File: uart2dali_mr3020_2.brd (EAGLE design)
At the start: 52 x 70 mm, 62 parts, among them IC1 SFH6156, IC2 SFH6156, IC4 7805DT, J1 AVR_SPI_PRG_6NS, Q1 BC817-25SMD, X2 SM04B-SRSS-TB

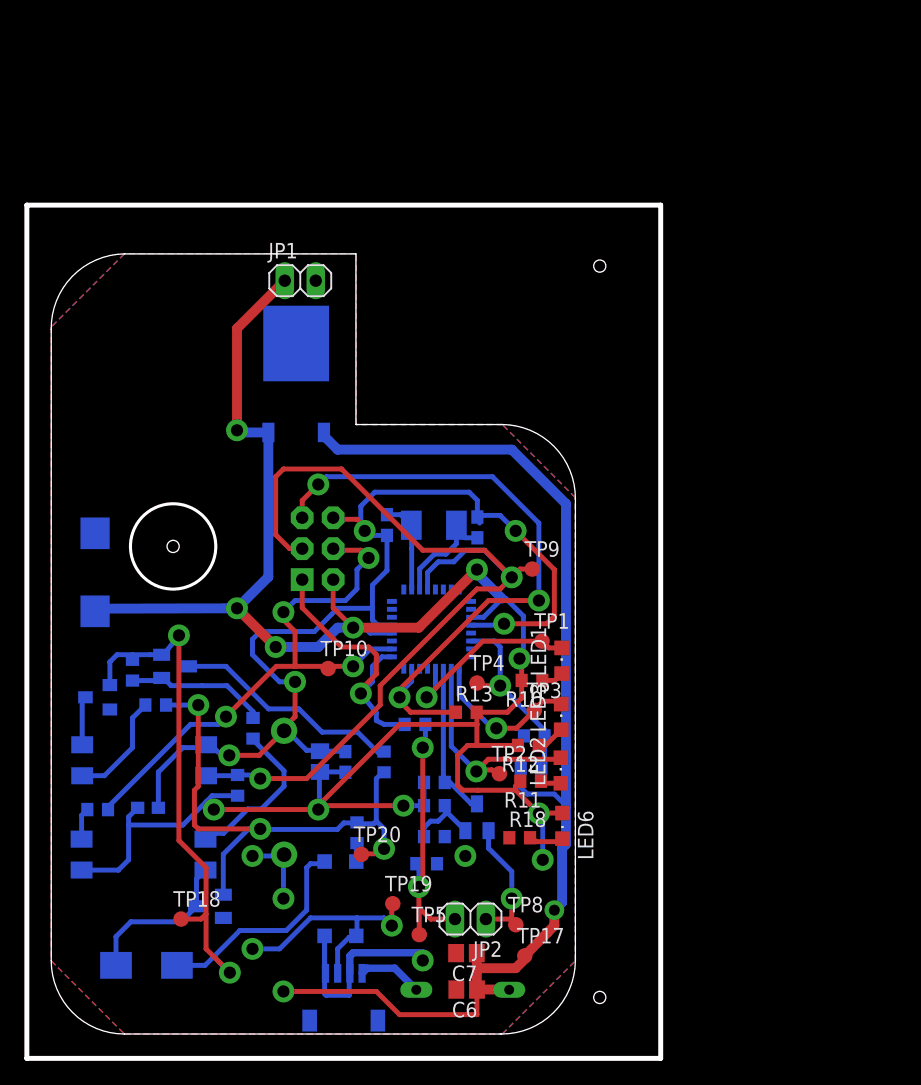
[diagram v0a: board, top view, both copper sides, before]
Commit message: working on uart2dali board version 2 with switching voltage regulators
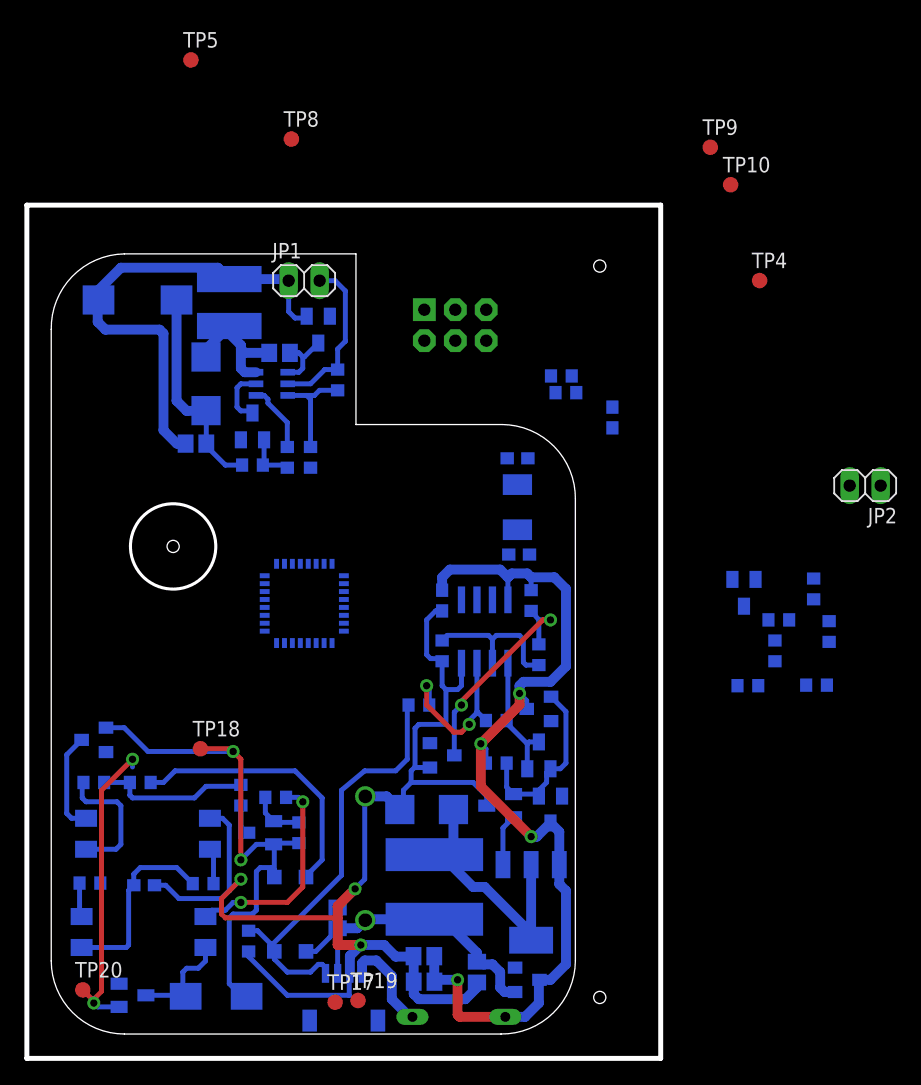
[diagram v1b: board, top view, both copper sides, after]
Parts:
- removed LED1, LED2, LED3, LED6: (no value), led:CHIPLED_0805
- removed TP1, TP2, TP3: TPB1,27, testpad:B1,27
- added C10: (no value), resistor:C0603
- added C11, C13: (no value), resistor:C0805
- added C12: (no value), resistor:CT6032
- added D10: BAS40, diode:SOT23
- added D11, D5, D6, D8: BZX84CSMD, diode:TO236
- added D7: MBRS130LT3, diode:SMB
- added D9: BZX85, diode:DO41Z10
- added IC3: SFH6156, optocoupler:SFH
- added Q2: BSP170P, transistor-fet:SOT223
- added Q3: BC817-25SMD, transistor-npn:SOT23-BEC
- added R22, R23, R24, R25, R26: (no value), resistor:R0603
- added T2, T3: (no value), transistor:SOT23-BEC
- added U$2: AT90PWM316, at90pwm316:QFN32_7MM
- added U$3: SDR0805, inductor:SDR0805
- C1: device resistor:CT6032 -> resistor:C0805
- C2, C3: device resistor:C0603 -> resistor:C0805
- C4: device resistor:CT7343 -> resistor:C0805
- C5: device resistor:C0603 -> resistor:CT7343
- C6, C7, C8: device resistor:C0805 -> resistor:C0603
- D1: value BAS40 -> 1N4148DO35-7; device diode:SOT23 -> diode:DO35-7
- D2: value BZX84CSMD -> BAS40; device diode:TO236 -> diode:SOT23
- D3: value BZX85 -> MBRS130LT3; device diode:DO41Z10 -> diode:SMB
- D4: value 1N4148DO35-7 -> BAS40; device diode:DO35-7 -> diode:SOT23
- IC1: value SFH6156 -> (none); device optocoupler:SFH -> ltc_swr:SOT23-6
- IC2: value SFH6156 -> LM393D; device optocoupler:SFH -> linear:SO08
- IC4: value 7805DT -> SFH6156; device linear:TO252 -> optocoupler:SFH
- Q1: value BC817-25SMD -> SST201; device transistor-npn:SOT23-BEC -> transistor-fet:SOT23
- R1, R2: device resistor:0204/7 -> resistor:R0603
- U$1: value AT90PWM316 -> KMP_2330_UNSHIELDED; device at90pwm316:QFN32_7MM -> inductor:KMP_2330_UNSHIELDED
- moved TP5 74.2 mm to (11.5, 79.9)
- moved TP8 67.0 mm to (19.7, 73.4)
- moved R8 57.1 mm to (59.4, 31.4), turned to 90 degrees
- moved R7 56.1 mm to (62.8, 28.6), turned to 0 degrees
- moved D4 55.4 mm to (21.9, 57.8), turned to 180 degrees
- moved TP10 51.6 mm to (55.7, 69.7)
- moved JP2 48.1 mm to (66.8, 45.0)
- moved R6 47.4 mm to (62.5, 36.5)
- moved R9 42.7 mm to (57.1, 28.6), turned to 0 degrees
- moved R5 42.1 mm to (63.8, 33.0)
- moved C5 41.7 mm to (7.08, 60.2)
- moved C7 40.8 mm to (38.3, 47.2), flipped to the bottom, turned to 0 degrees
- moved TP4 40.3 mm to (58.1, 61.8)
- moved IC1 40.0 mm to (18.1, 53.3)
- moved IC4 39.6 mm to (7.94, 16.4), turned to 270 degrees
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- renumbered X2 to X1
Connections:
- removed net N$13: B1.-, R5.1
- removed net N$14: LED2.A, R11.1
- removed net N$15: LED3.A, R12.1
- removed net N$21: R20.1, T1.C, U$1.P27
- removed net N$27: LED3.C, TP3.TP, U$1.P25
- removed net N$28: LED2.C, TP2.TP, U$1.P26
- removed net N$29: LED1.C, TP1.TP, U$1.P28
- removed net N$30: R16.1, R17.2, TP4.TP, U$1.P22
- removed net N$32: LED6.C, R18.2
- removed net N$7: B1.+, C1.-, D2.A, Q1.E, R7.2, TP18.TP
- removed net N$8: LED1.A, R10.1
- new net D+: B1.+, C12.-, D11.A, Q3.E, R22.2, TP18.TP
- new net D-: B1.-, R23.1
- new net GNDA: B1.~2, R17.1, R19.2, X1.4
- new net N$18: IC1.4, R2.1
- new net N$22: IC2.1, Q1.2, Q1.3, R16.1
- new net N$24: C3.1, D4.3, IC1.1
- new net N$25: C3.2, D3.C, IC1.6, U$1.P$2
- new net N$26: D7.C, Q2.2, Q2.4, U$3.P$2
- new net N$31: IC1.3, R3.2, R4.2
- new net N$33: Q2.1, T2.E, T3.E
- new net N$34: D6.A, Q1.1, R18.1, T2.B, T3.B
- new net N$35: D5.C, R13.1, R14.1
- new net N$40: IC2.3, R16.2, R17.2
- new net SOFT_RXD_5V: R10.1, T1.C, U$2.P27
- new net VCC/2: B1.~1, C11.1, C13.2, D8.A, D9.C, TP19.TP, U$3.P$1, X1.3
- new net V_SENSE: R11.1, R12.2, TP4.TP, U$2.P22
- net +5V: now also C4.2, C5.+, C6.2, D4.1, IC3.1, R26.1, R4.1, R7.2, R9.2, U$1.P$1, U$2.P19, U$2.P4; no longer C4.+, C5.2, C8.2, IC1.1, IC4.2, LED6.A, R11.2, R12.2, R13.2, R19.2, R20.2, R9.1, U$1.P19, U$1.P4
- net DALI_RCV: now also IC4.4, R26.2, U$2.P12; no longer IC2.4, R9.2, U$1.P12
- net DALI_TRM: now also R20.1, U$2.P2; no longer R8.1, U$1.P2
- net GND: now also C1.2, C10.2, C11.2, C13.1, C2.2, C4.1, C5.-, C6.1, C7.1, D5.A, D7.A, D9.A, IC1.2, IC2.4, R1.2, R12.1, R15.2, R19.1, R3.1, R5.1, R8.2, T3.C, U$2.P20, U$2.P5; no longer B1.~2, C2.1, C3.1, C4.-, C5.1, C6.2, C7.2, IC2.3, R15.1, R17.1, R18.1, R21.2, U$1.P20, U$1.P5, X1.4
- net MISO: now also R6.2, U$2.P1; no longer R14.2, U$1.P1
- net N$1: now also IC3.2, R20.2; no longer IC1.2, R8.2
- net N$10: now also Q3.C, R24.2; no longer Q1.C, R3.2
- net N$11: now also IC4.1, R25.1; no longer IC2.1, R4.1
- net N$12: now also D11.C, IC4.2; no longer D2.C, IC2.2
- net N$16: now also C7.2, U$2.P10; no longer C2.2, U$1.P10
- net N$19: now also C8.2, U$2.P11; no longer C3.2, U$1.P11
- net N$2: now also IC2.2, R14.2, R15.1; no longer B1.~1, R2.1, TP19.TP, X1.3
- net N$20: now also R8.1, R9.1; no longer R19.1, R21.1
- net N$23: now also D1.A; no longer D4.A
- net N$3: now also D2.3, IC1.5; no longer D3.C, R1.1, R2.2
- net N$4: now also C12.+, D10.3, IC3.4; no longer C1.+, D1.3, IC1.4
- net N$5: now also IC3.3, R21.1; no longer IC1.3, R6.1
- net N$6: now also Q3.B, R21.2, R22.1; no longer Q1.B, R6.2, R7.1
- net N$9: now also D10.1, R23.2, R24.1, R25.2; no longer D1.1, R3.1, R4.2, R5.2
- net RESET: now also R7.1, U$2.P31; no longer R13.1, U$1.P31
- net SOFT_TXD: now also R5.2, R6.1; no longer R14.1, R15.2
- net VDD: now also C1.1, C10.1, C2.1, D1.C, D2.1, D6.C, D8.C, IC2.8, Q2.3, R1.1, R11.2, R13.2, R18.2, R2.2, T2.C; no longer C6.1, C7.1, D4.C, IC4.1, R1.2, R16.2
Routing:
- net +5V: track 181.3 -> 55.3 mm, vias 11 -> 0
- net DALI_RCV: track 75.7 -> 2.94 mm, vias 2 -> 0
- net N$7: track 60.2 -> 0.00 mm, vias 2 -> 0
- net RESET: track 52.7 -> 0.00 mm, vias 3 -> 0
- net DALI_TRM: track 47.3 -> 0.00 mm, vias 4 -> 0
- net D+: track 0.00 -> 46.4 mm, vias 0 -> 2
- net GNDA: track 0.00 -> 35.4 mm
- net GND: track 110.9 -> 143.1 mm, vias 7 -> 3
- net VCC/2: track 0.00 -> 25.6 mm
- net MISO: track 23.3 -> 0.00 mm, vias 1 -> 0
- net SOFT_TXD: track 22.7 -> 0.00 mm, vias 2 -> 0
- net D-: track 0.00 -> 22.4 mm
- net N$26: track 0.00 -> 21.8 mm
- net N$35: track 0.00 -> 18.7 mm, vias 0 -> 2
- net N$28: track 18.5 -> 0.00 mm, vias 1 -> 0
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- removed copper zone on layer 1, net GND
- removed copper zone on layer 16, net GND

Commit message: new version of the base board with 2 switching regulators
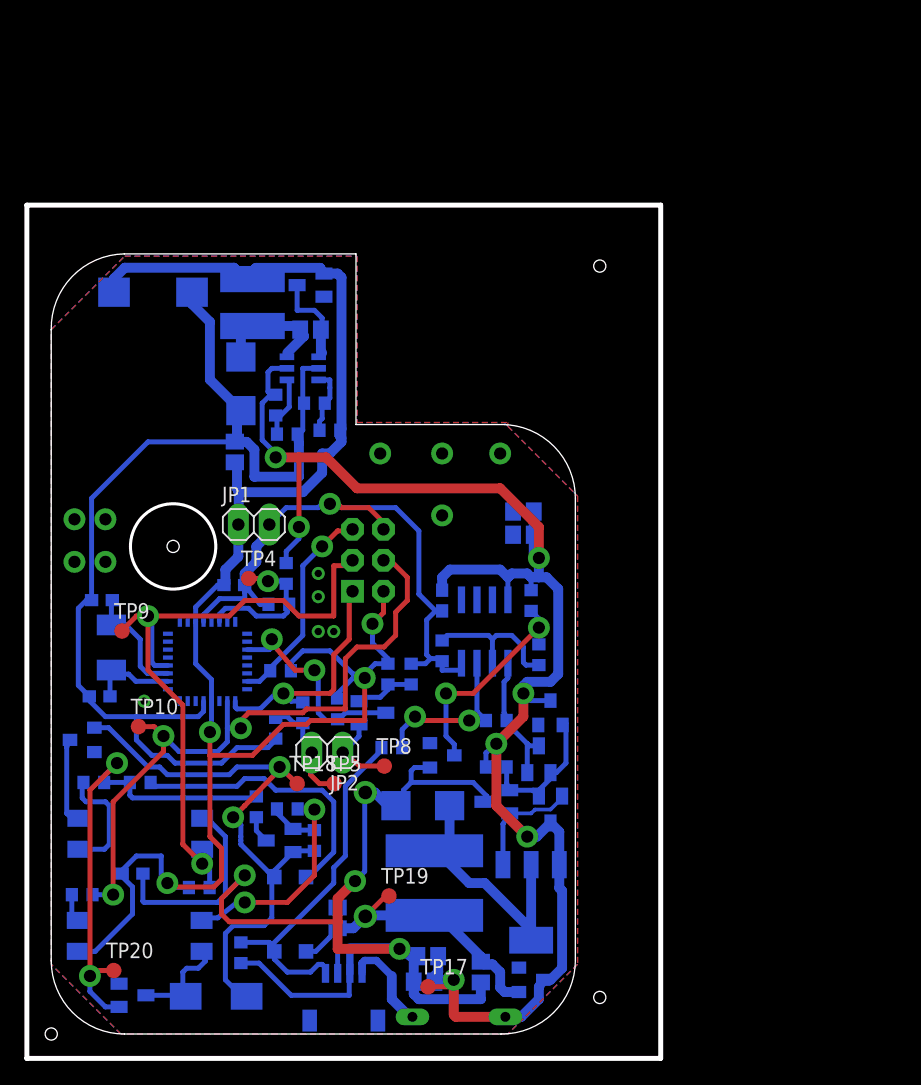
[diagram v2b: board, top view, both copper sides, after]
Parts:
- removed D2: BAS40, diode:SOT23
- added C14, C15: (no value), resistor:C0805
- R1: value (none) -> 10k
- R2: value (none) -> 47k
- R3: value (none) -> 27k
- R4: value (none) -> 82k
- moved TP10 65.8 mm to (7.16, 25.2)
- moved TP9 62.5 mm to (5.81, 33.1)
- moved TP5 60.5 mm to (23.2, 20.5)
- moved TP8 52.0 mm to (27.3, 22.0)
- moved JP2 49.3 mm to (22.6, 23.1)
- moved TP4 48.5 mm to (16.2, 37.4)
- moved R5 46.1 mm to (18.4, 25.1)
- moved R7 44.0 mm to (18.8, 29.8), turned to 180 degrees
- moved R6 43.1 mm to (20.6, 26.4)
- moved C7 39.5 mm to (3.97, 27.7), turned to 180 degrees
- moved R10 36.9 mm to (23.5, 26.7), turned to 90 degrees
- moved Y1 35.2 mm to (4.93, 31.7), turned to 270 degrees
- moved C8 34.4 mm to (4.16, 35.6), turned to 180 degrees
- moved C9 33.9 mm to (15.0, 36.8), turned to 180 degrees
- moved T1 32.0 mm to (26.4, 26.4), turned to 90 degrees
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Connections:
- removed net N$18: IC1.4, R2.1
- net GND: now also C14.2, C15.2
- net N$3: now also IC1.4, R1.1, R2.1; no longer D2.3, IC1.5
- net VDD: now also C14.1, C15.1, IC1.5; no longer D2.1, R1.1
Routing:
- net GND: track 143.1 -> 244.0 mm, vias 3 -> 17
- net +5V: track 55.3 -> 144.1 mm, vias 0 -> 4
- net DALI_TRM: track 0.00 -> 55.7 mm, vias 0 -> 3
- net DALI_RCV: track 2.94 -> 56.7 mm, vias 0 -> 2
- net VDD: track 81.9 -> 130.6 mm, vias 4 -> 7
- net MISO: track 0.00 -> 20.2 mm, vias 0 -> 1
- net SOFT_RXD_5V: track 0.00 -> 17.4 mm, vias 0 -> 2
- net RESET: track 0.00 -> 17.3 mm, vias 0 -> 1
- net V_SENSE: track 0.00 -> 13.2 mm, vias 0 -> 1
- net SOFT_TXD: track 0.00 -> 9.71 mm
- net N$19: track 0.00 -> 9.65 mm
- net N$16: track 0.00 -> 7.22 mm
- net SOFT_RXD: track 0.00 -> 6.66 mm
- net GNDA: track 35.4 -> 29.6 mm
- net N$18: track 5.69 -> 0.00 mm
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- added copper zone on layer 1, net GND
- added copper zone on layer 16, net GND

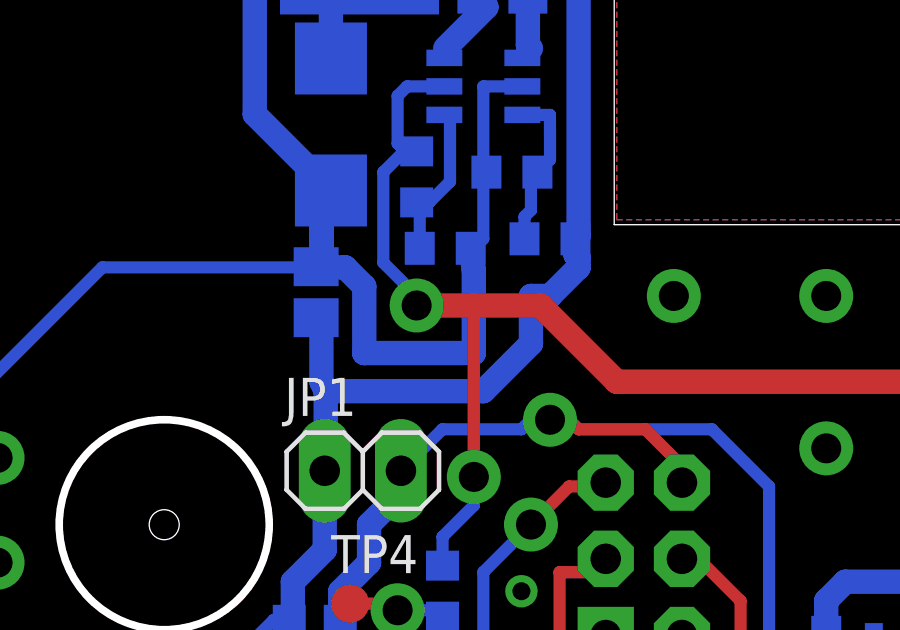
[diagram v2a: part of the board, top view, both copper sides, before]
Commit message: - fixed mispelling in dali_encode - added dali_encode to SConstruct - minor fixes on schematics and board
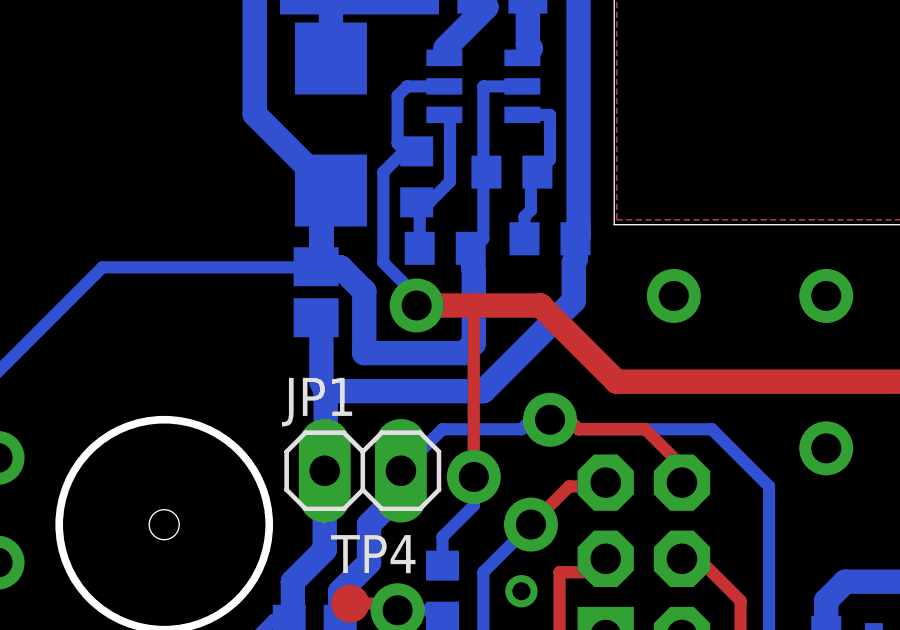
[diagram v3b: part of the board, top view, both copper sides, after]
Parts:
- D11: value BZX84CSMD -> BZX84CSMD 2V7
- R24: value (none) -> 4R7
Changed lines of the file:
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@@
 <setting verticaltext="up"/>
 </settings>
-<grid distance="0.00625" unitdist="inch" unit="inch" style="lines" multiple="1" display="yes" altdistance="0.025" altunitdist="inch" altunit="inch"/>
+<grid distance="0.0125" unitdist="inch" unit="inch" style="lines" multiple="1" display="yes" altdistance="0.025" altunitdist="inch" altunit="inch"/>
 <layers>
 <layer number="1" name="Top" color="4" fill="1" visible="yes" active="yes"/>
@@
 <rectangle x1="27.305" y1="7.9375" x2="35.56" y2="16.1925" layer="41"/>
 <hole x="0" y="0" drill="1"/>
+<rectangle x1="13.6525" y1="56.8325" x2="19.3929" y2="63.8175" layer="41"/>
+<rectangle x1="13.6525" y1="56.8325" x2="19.3929" y2="63.8175" layer="42"/>
 </plain>
 <attributes>
@@
 <element name="Q3" library="transistor-npn" package="SOT23-BEC" value="BC817-25SMD" x="18.7325" y="15.875" rot="MR270"/>
 <element name="D10" library="diode" package="SOT23" value="BAS40" x="6.6675" y="3.175" rot="MR90"/>
-<element name="D11" library="diode" package="TO236" value="BZX84CSMD" x="2.54" y="24.13" rot="MR270"/>
+<element name="D11" library="diode" package="TO236" value="BZX84CSMD 2V7" x="2.54" y="24.13" rot="MR270"/>
 <element name="D9" library="diode" package="DO41Z10" value="BZX85" x="25.765" y="14.7325" rot="MR90"/>
 <element name="R25" library="resistor" package="R0603" value="" x="3.4925" y="20.6375" rot="MR180"/>
 <element name="R23" library="resistor" package="R0603" value="" x="7.3025" y="20.6375" rot="MR0"/>
-<element name="R24" library="resistor" package="R0603" value="" x="16.8275" y="18.6375" rot="MR270"/>
+<element name="R24" library="resistor" package="R0603" value="4R7" x="16.8275" y="18.6375" rot="MR270"/>
 <element name="R21" library="resistor" package="R0603" value="" x="19.3675" y="18.4625" rot="MR0"/>
 <element name="R22" library="resistor" package="R0603" value="" x="21.59" y="15.875" rot="MR270"/>
@@
 <wire x1="15.5575" y1="51.14" x2="15.24" y2="50.4825" width="0.8128" layer="16"/>
 <wire x1="15.24" y1="50.4825" x2="15.24" y2="48.5775" width="0.8128" layer="16"/>
-<wire x1="15.24" y1="48.5775" x2="16.03375" y2="48.5775" width="0.8128" layer="16"/>
-<wire x1="16.03375" y1="48.5775" x2="16.66875" y2="47.9425" width="0.8128" layer="16"/>
-<wire x1="16.66875" y1="47.9425" x2="16.66875" y2="45.72" width="0.8128" layer="16"/>
-<wire x1="16.66875" y1="45.72" x2="20.32" y2="45.72" width="0.8128" layer="16"/>
-<wire x1="20.32" y1="45.72" x2="20.32" y2="48.475" width="0.8128" layer="16"/>
+<wire x1="15.24" y1="48.5775" x2="15.875" y2="48.5775" width="0.8128" layer="16"/>
+<wire x1="15.875" y1="48.5775" x2="16.66875" y2="47.78375" width="0.8128" layer="16"/>
+<wire x1="16.66875" y1="47.78375" x2="16.66875" y2="45.72" width="0.8128" layer="16"/>
+<wire x1="16.66875" y1="45.72" x2="20.0025" y2="45.72" width="0.8128" layer="16"/>
+<wire x1="20.0025" y1="45.72" x2="20.32" y2="46.0375" width="0.8128" layer="16"/>
+<wire x1="20.32" y1="46.0375" x2="20.32" y2="48.475" width="0.8128" layer="16"/>
 <wire x1="20.32" y1="48.475" x2="20.2175" y2="49.2125" width="0.8128" layer="16"/>
 <wire x1="15.8675" y1="36.83" x2="15.8675" y2="37.775" width="0.8128" layer="16"/>
@@
 <wire x1="23.8125" y1="62.07125" x2="23.8125" y2="49.6325" width="0.8128" layer="16"/>
 <wire x1="23.8125" y1="49.6325" x2="23.71" y2="49.53" width="0.8128" layer="16"/>
-<wire x1="23.71" y1="49.53" x2="23.71" y2="48.9975" width="0.8128" layer="16"/>
-<wire x1="23.71" y1="48.9975" x2="23.8125" y2="48.895" width="0.8128" layer="16"/>
-<wire x1="23.8125" y1="48.895" x2="23.8125" y2="48.5775" width="0.8128" layer="16"/>
-<wire x1="23.8125" y1="48.5775" x2="22.86" y2="47.625" width="0.8128" layer="16"/>
-<wire x1="22.86" y1="47.625" x2="22.225" y2="47.625" width="0.8128" layer="16"/>
-<wire x1="22.225" y1="47.625" x2="22.225" y2="46.0375" width="0.8128" layer="16"/>
-<wire x1="22.225" y1="46.0375" x2="20.6375" y2="44.45" width="0.8128" layer="16"/>
+<wire x1="23.71" y1="49.53" x2="23.71" y2="48.83875" width="0.8128" layer="16"/>
+<wire x1="23.71" y1="48.83875" x2="23.65375" y2="48.73625" width="0.8128" layer="16"/>
+<wire x1="23.65375" y1="48.73625" x2="23.65375" y2="47.46625" width="0.8128" layer="16"/>
+<wire x1="23.65375" y1="47.46625" x2="20.6375" y2="44.45" width="0.8128" layer="16"/>
 <wire x1="20.6375" y1="44.45" x2="15.3825" y2="44.45" width="0.8128" layer="16"/>
 <wire x1="14.1675" y1="36.83" x2="13.6525" y2="36.83" width="0.4064" layer="16"/>
@@
 <wire x1="18.415" y1="52.3875" x2="18.3125" y2="52.3875" width="0.4064" layer="16"/>
 <wire x1="18.3125" y1="52.3875" x2="18.415" y2="52.44375" width="0.4064" layer="16"/>
-<wire x1="18.5175" y1="47.5225" x2="18.415" y2="47.3075" width="0.8128" layer="16"/>
+<wire x1="18.35875" y1="47.68125" x2="18.415" y2="47.3075" width="0.8128" layer="16"/>
 <via x="18.415" y="47.3075" extent="1-16" drill="1" shape="square"/>
 <wire x1="18.415" y1="47.3075" x2="20.32" y2="47.3075" width="0.8128" layer="1"/>
@@
 <wire x1="39.585" y1="40.9575" x2="39.585" y2="39.4725" width="0.8128" layer="16"/>
 <wire x1="39.585" y1="39.4725" x2="40.005" y2="39.0525" width="0.8128" layer="16"/>
-<wire x1="18.5175" y1="47.5225" x2="17.30375" y2="48.73625" width="0.4064" layer="16"/>
+<wire x1="18.35875" y1="47.68125" x2="17.30375" y2="48.73625" width="0.4064" layer="16"/>
 <wire x1="17.30375" y1="48.73625" x2="17.30375" y2="51.7525" width="0.4064" layer="16"/>
 <wire x1="17.30375" y1="51.7525" x2="18.018125" y2="52.466875" width="0.4064" layer="16"/>
